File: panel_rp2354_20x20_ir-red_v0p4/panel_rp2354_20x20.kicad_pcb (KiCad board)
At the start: 6 copper layers, 45 x 45 mm, 557 parts, among them J1 Conn_01x04, J2 Conn_01x05, J3 Conn_01x05, J4 Conn_01x05, J5 Conn_01x05, SW1 SW_Push, SW2 SW_Push, U1 APS6404L-3SQR, U10 UCC27517, U11 UCC27517, U12 UCC27517, U13 UCC27517, U14 UCC27517, U15 UCC27517, U16 UCC27517, U17 UCC27517, U18 UCC27517, U19 UCC27517, U2 RP2354B_80QFN, U20 UCC27517, U21 UCC27517, U22 UCC27517, U23 UCC27517, U24 UCC27517, U25 UCC27517, U26 UCC27517, U27 UCC27517, U28 UCC27517, U29 UCC27517, U3 UCC27517, U30 UCC27517, U31 UCC27517, U32 UCC27517, U33 UCC27517, U34 UCC27517, U35 UCC27517, U36 UCC27517, U37 UCC27517, U38 UCC27517, U39 UCC27517, U4 UCC27517, U40 UCC27517, U41 UCC27517, U42 UCC27517, U43 AP2112K-3.3, U5 UCC27517, U6 UCC27517, U7 UCC27517, U8 UCC27517, U9 UCC27517, Y1 ABM8-272-T3

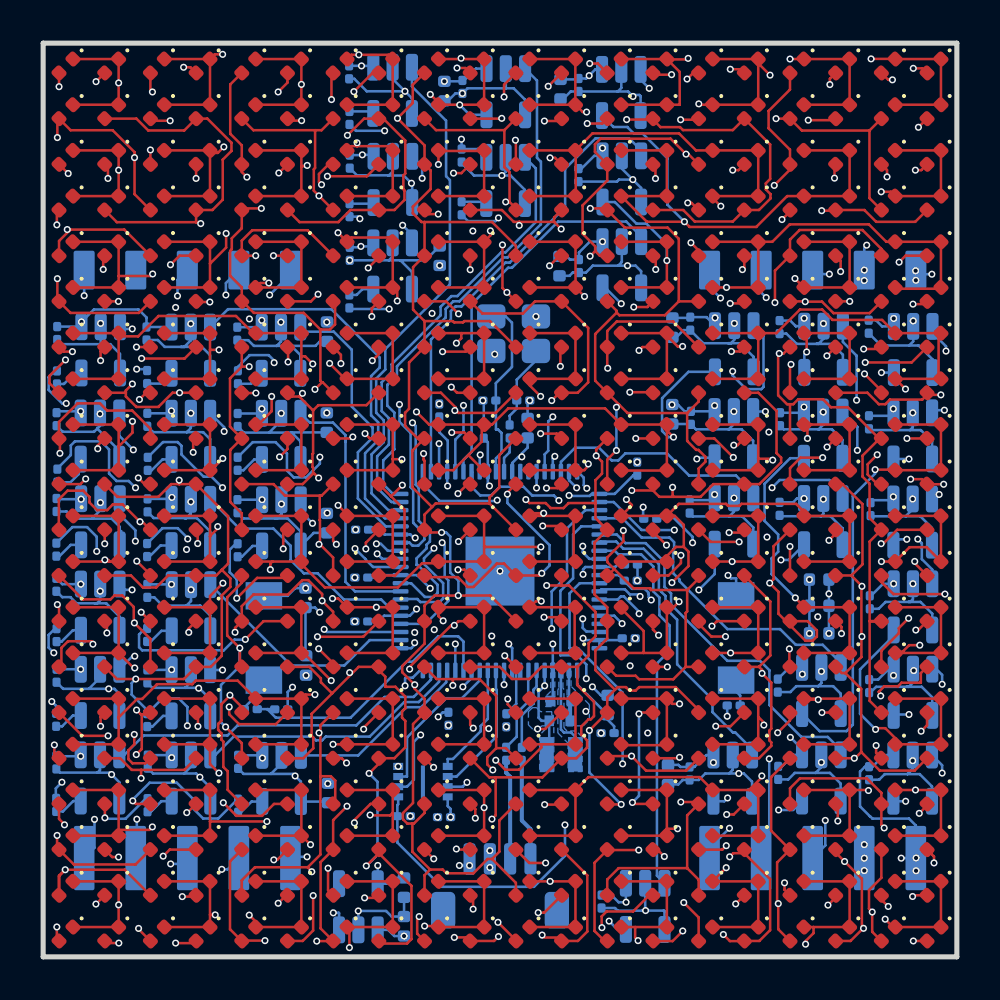
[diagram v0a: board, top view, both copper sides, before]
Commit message: IR-red panel v0.4r2: checkerboard, 33/56 Ω 0.2 W 0402 column resistors
- LED banks: T2 -> IR (C6879329), T3 -> red (C2852592); red is now T0+T3
  (checkerboard, firmware channels 0 and 3), IR T1+T2. BOM-only change.
- R9-R28: Resistor_SMD:R_0201_0603Metric -> R_0402_1005Metric, same
  rotation and side. Red banks 33 Ω (Panasonic ERJ-PA2F33R0X, C427231),
  IR banks 56 Ω (ERJ-PA2F56R0X, C427233; 0 stock at JLC on 2026-09-26,
  alternates listed in CHANGES-v0p4r2.md). Vishay CRCW-HP codes noted.
- Layout: nine resistor centres nudged 0.03-0.20 mm, ten vias moved, six
  short track re-routes so every 0402 pad has >= 0.135 mm to foreign
  copper; no driver or other part moved. DRC at 0.127 mm clearance has
  the same 68 pre-existing 0.125 mm netclass items as v0.4r1, 0
  unconnected, plus 19 courtyard overlaps (0402 vs SOT-23-5 courtyards).
- production/v0p4r2 regenerated with Fabrication Toolkit 5.3.1; board rev
  v0.4.2. Scripts used are in tools/column_resistors_0402 and apply to
  the four-color and v0.3 boards (identical layouts).

Co-Authored-By: Claude Fable 5.1 <noreply@anthropic.com>
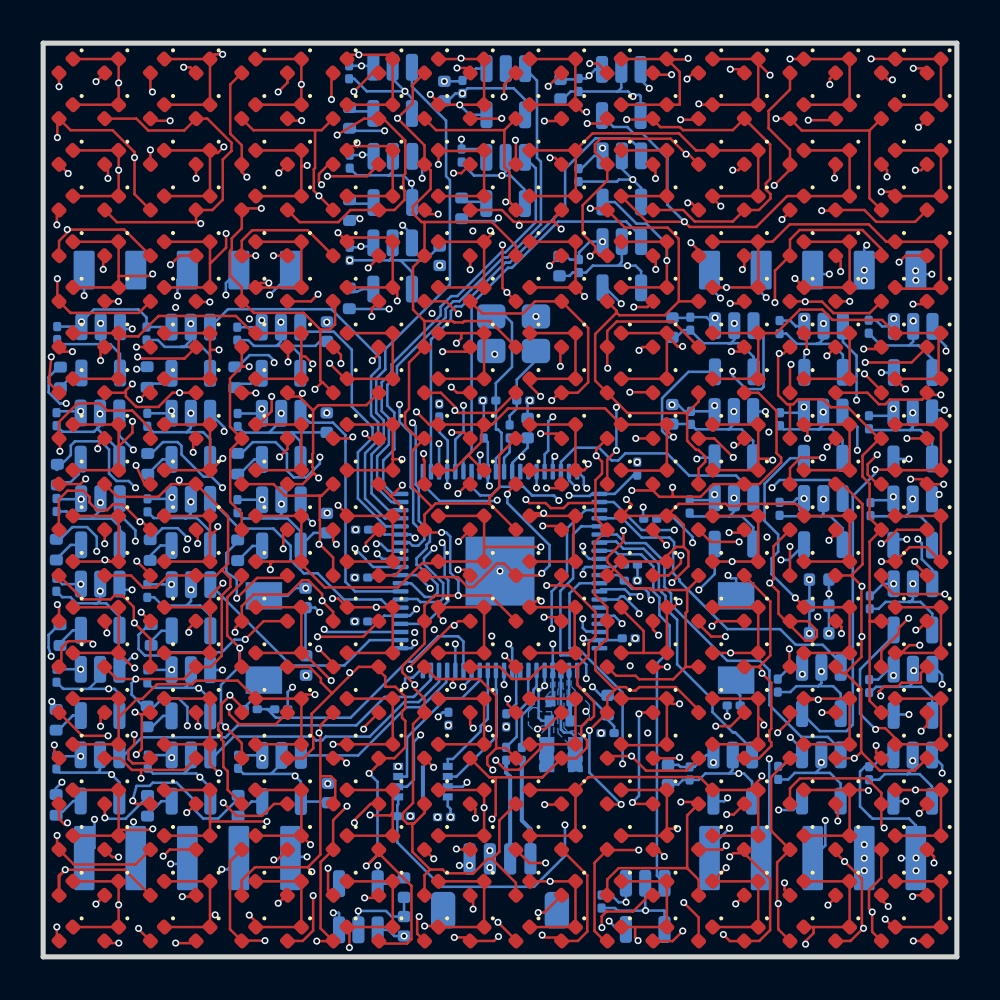
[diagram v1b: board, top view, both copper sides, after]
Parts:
- R10, R11, R12, R13, R14, R15, R16, R17, R18, R19, R20, R21, R22, R23, R24, R25, R26, R27, R28, R9: footprint Resistor_SMD:R_0201_0603Metric -> Resistor_SMD:R_0402_1005Metric
- moved R14 0.20 mm to (55.3, 79.1)
- moved R12 0.18 mm to (55.1, 83.2)
- moved R15 0.17 mm to (50.8, 79.2)
- moved R22 0.17 mm to (50.9, 66.5)
- moved R17 0.15 mm to (55.3, 75.0)
- moved R25 0.15 mm to (59.4, 66.5)
- moved R24 0.15 mm to (65.1, 62.6)
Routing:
- net Net-(D41-A): track 114.5 -> 115.1 mm
